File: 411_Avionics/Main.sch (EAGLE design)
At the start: 26 parts, among them CN1 Battery Connector, IC1 BQ24022, IC3 74AC11138D, T1 NTR1P02, T2 NTR1P02, U1 USB_In, U2 ATTINY85V-10SU, U3 LSM9DS0, U5 LM317DCY

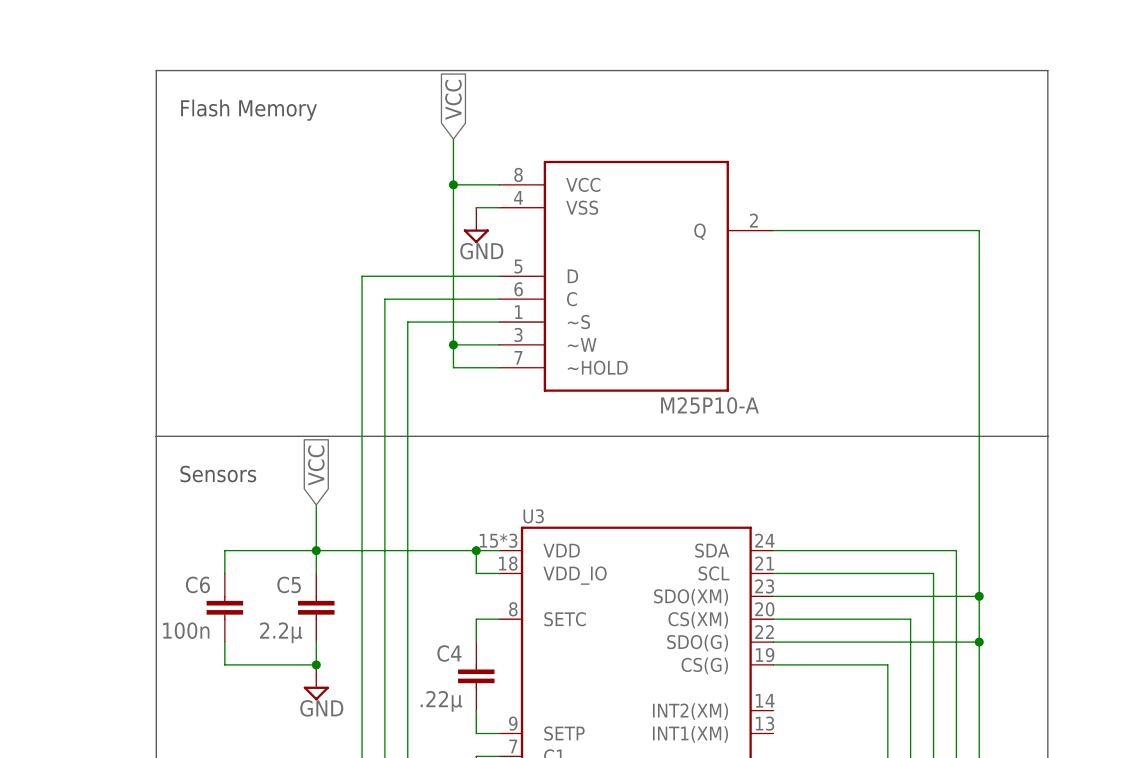
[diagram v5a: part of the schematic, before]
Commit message: Added pin headers to read memory contents. Change before release!
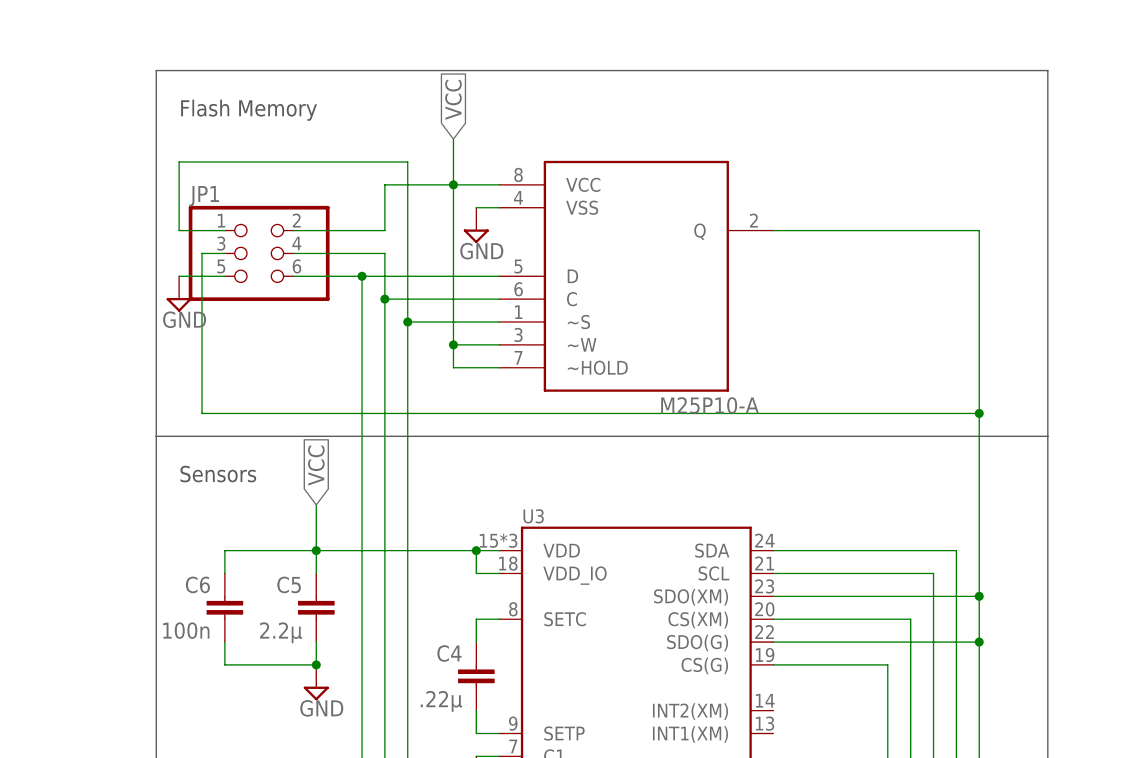
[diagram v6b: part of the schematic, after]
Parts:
- added JP1: (no value), pinhead:PINHD-2X3
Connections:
- net CLK: now also JP1.4
- net GND: now also JP1.5
- net MEM_EN: now also JP1.1
- net MISO: now also JP1.3
- net MOSI: now also JP1.6
- net N$3: now also JP1.2
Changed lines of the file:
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@@
 <part name="C10" library="rcl" deviceset="C-EU" device="C0805" value="100n"/>
 <part name="SUPPLY16" library="supply2" deviceset="GND" device=""/>
+<part name="JP1" library="pinhead" deviceset="PINHD-2X3" device=""/>
+<part name="SUPPLY17" library="supply2" deviceset="GND" device=""/>
 </parts>
 <sheets>
@@
 <instance part="C10" gate="G$1" x="170.18" y="246.38" rot="MR0"/>
 <instance part="SUPPLY16" gate="GND" x="170.18" y="238.76"/>
+<instance part="JP1" gate="A" x="269.24" y="220.98"/>
+<instance part="SUPPLY17" gate="GND" x="261.62" y="215.9"/>
 </instances>
 <busses>
@@
 <pinref part="SUPPLY16" gate="GND" pin="GND"/>
 </segment>
+<segment>
+<pinref part="JP1" gate="A" pin="5"/>
+<wire x1="266.7" y1="218.44" x2="261.62" y2="218.44" width="0.1524" layer="91"/>
+<pinref part="SUPPLY17" gate="GND" pin="GND"/>
+</segment>
 </net>
 <net name="N$4" class="0">
@@
 <wire x1="254" y1="127" x2="284.48" y2="127" width="0.1524" layer="91"/>
 <label x="269.24" y="127" size="1.778" layer="95"/>
+<wire x1="284.48" y1="215.9" x2="284.48" y2="220.98" width="0.1524" layer="91"/>
+<junction x="284.48" y="215.9"/>
+<pinref part="JP1" gate="A" pin="4"/>
+<wire x1="284.48" y1="220.98" x2="274.32" y2="220.98" width="0.1524" layer="91"/>
 </segment>
 </net>
@@
 <pinref part="U$1" gate="G$1" pin="Q"/>
 <wire x1="350.52" y1="177.8" x2="350.52" y2="182.88" width="0.1524" layer="91"/>
-<wire x1="350.52" y1="182.88" x2="350.52" y2="223.52" width="0.1524" layer="91"/>
+<wire x1="350.52" y1="182.88" x2="350.52" y2="203.2" width="0.1524" layer="91"/>
+<wire x1="350.52" y1="203.2" x2="350.52" y2="223.52" width="0.1524" layer="91"/>
 <wire x1="350.52" y1="223.52" x2="327.66" y2="223.52" width="0.1524" layer="91"/>
 <pinref part="U3" gate="G$1" pin="SDO(XM)"/>
@@
 <junction x="350.52" y="177.8"/>
 <label x="269.24" y="129.54" size="1.778" layer="95"/>
+<wire x1="350.52" y1="203.2" x2="264.16" y2="203.2" width="0.1524" layer="91"/>
+<junction x="350.52" y="203.2"/>
+<wire x1="264.16" y1="203.2" x2="264.16" y2="220.98" width="0.1524" layer="91"/>
+<pinref part="JP1" gate="A" pin="3"/>
+<wire x1="264.16" y1="220.98" x2="266.7" y2="220.98" width="0.1524" layer="91"/>
 </segment>
 </net>
@@
 <wire x1="347.98" y1="187.96" x2="327.66" y2="187.96" width="0.1524" layer="91"/>
 <label x="269.24" y="132.08" size="1.778" layer="95"/>
+<pinref part="JP1" gate="A" pin="6"/>
+<wire x1="274.32" y1="218.44" x2="281.94" y2="218.44" width="0.1524" layer="91"/>
+<junction x="281.94" y="218.44"/>
 </segment>
 </net>
@@
 <wire x1="337.82" y1="119.38" x2="325.12" y2="119.38" width="0.1524" layer="91"/>
 <label x="327.66" y="119.38" size="1.778" layer="95"/>
+<wire x1="287.02" y1="213.36" x2="287.02" y2="231.14" width="0.1524" layer="91"/>
+<junction x="287.02" y="213.36"/>
+<wire x1="287.02" y1="231.14" x2="261.62" y2="231.14" width="0.1524" layer="91"/>
+<wire x1="261.62" y1="231.14" x2="261.62" y2="223.52" width="0.1524" layer="91"/>
+<pinref part="JP1" gate="A" pin="1"/>
+<wire x1="261.62" y1="223.52" x2="266.7" y2="223.52" width="0.1524" layer="91"/>
 </segment>
 </net>
@@
 <wire x1="297.18" y1="228.6" x2="292.1" y2="228.6" width="0.1524" layer="91"/>
 <junction x="292.1" y="228.6"/>
-</segment>
-</net>
+<pinref part="JP1" gate="A" pin="2"/>
+<wire x1="274.32" y1="223.52" x2="284.48" y2="223.52" width="0.1524" layer="91"/>
+<wire x1="284.48" y1="223.52" x2="284.48" y2="228.6" width="0.1524" layer="91"/>
+<wire x1="284.48" y1="228.6" x2="292.1" y2="228.6" width="0.1524" layer="91"/>
+</segment>
+</net>

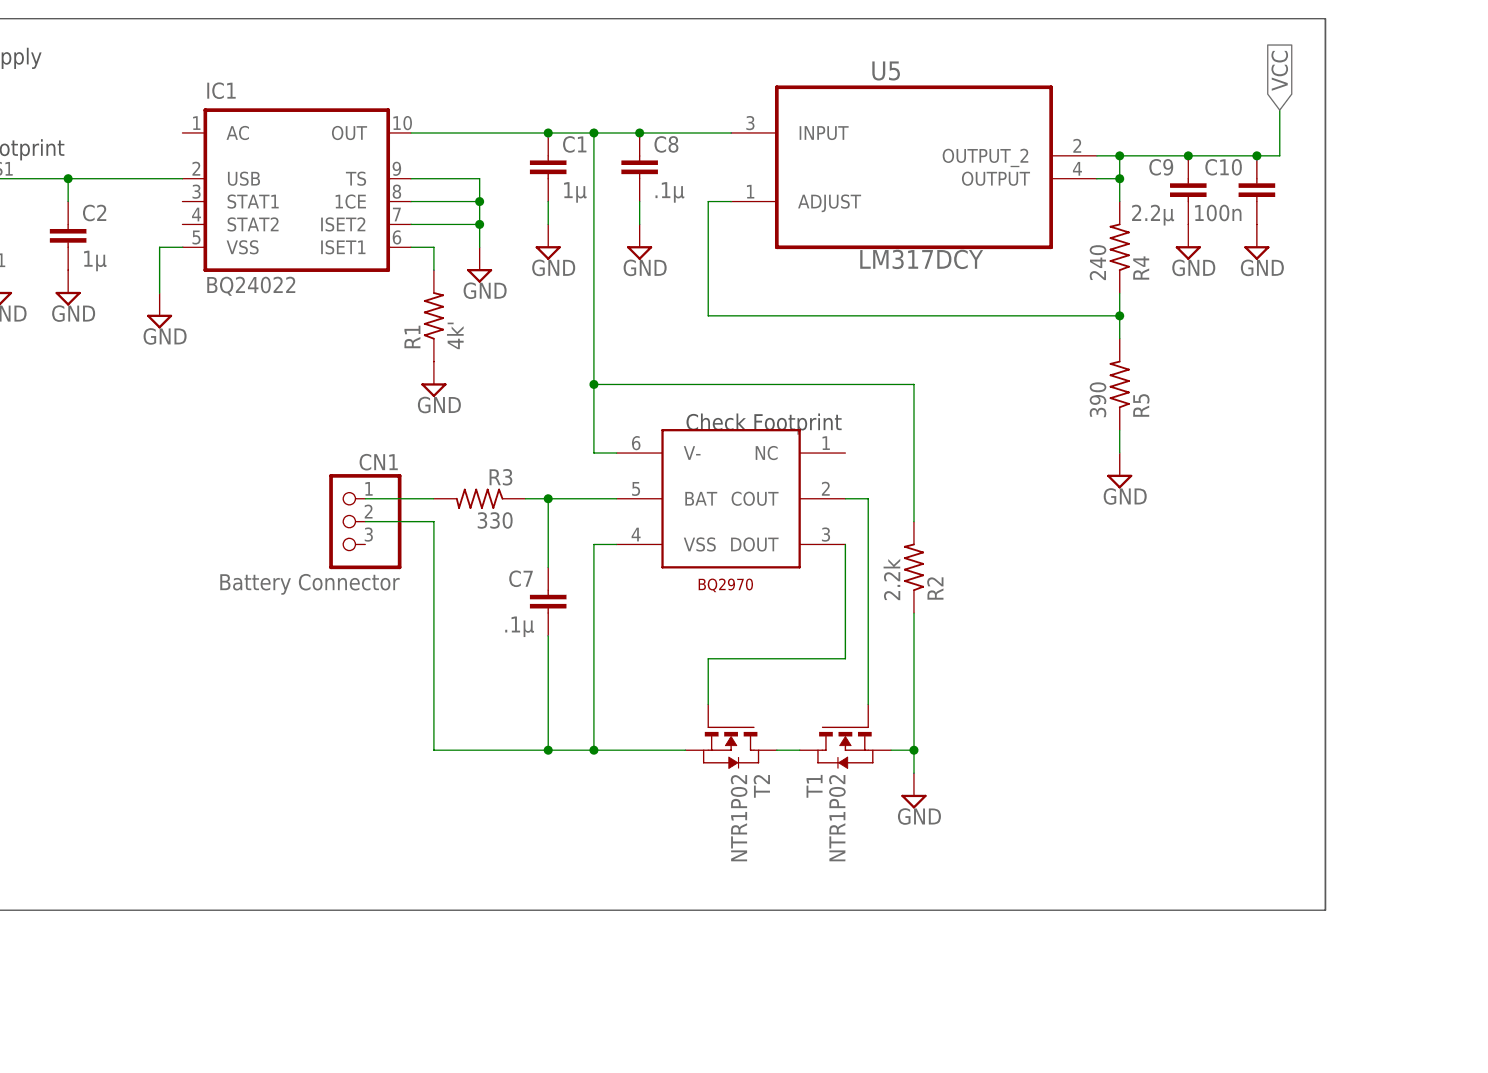
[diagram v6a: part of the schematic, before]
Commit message: ECE411: Began reworking schematic, removed cell protection and added LDO to library and schematic.
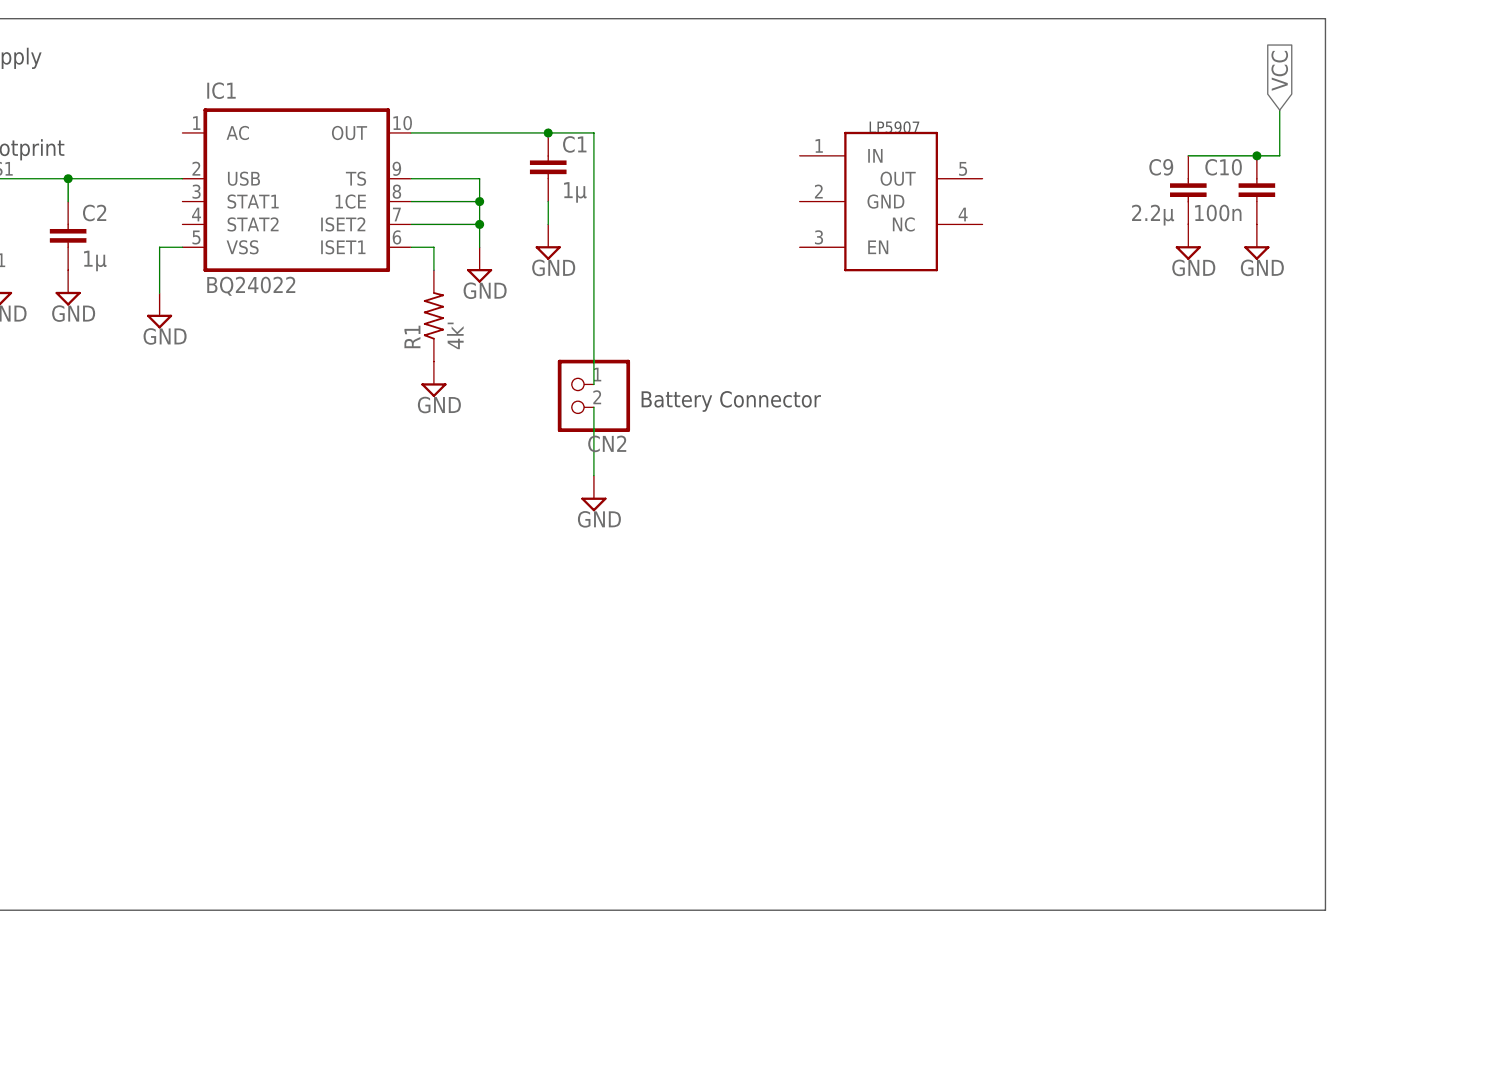
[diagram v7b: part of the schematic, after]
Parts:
- removed C7: .1µ, rcl:C-EUC0805
- removed C8: .1µ, rcl:C-EU050-025X075
- removed CN1: Battery Connector, adafruit:JST_3PIN
- removed R2: 2.2k, resistor:R-US_R0805
- removed R3: 330, resistor:R-US_R0805
- removed R4: 240, resistor:R-US_R0805
- removed R5: 390, resistor:R-US_R0805
- removed T1, T2: NTR1P02, zetex:NMOSSOT23
- removed U5: LM317DCY, LM317DCY:LM317DCY
- added CN2: (no value), adafruit:JST_2PIN-SMT-RA
- U$2: value BQ2970 -> LP5907; device WSON-6-PAD:BQ2970 -> adafruit:LP5907
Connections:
- removed net N$12: T1.G, U$2.COUT
- removed net N$13: T2.G, U$2.DOUT
- removed net N$14: T1.D, T2.D
- removed net N$15: C7.1, R3.1, U$2.BAT
- removed net N$16: C7.2, CN1.2, T2.S, U$2.VSS
- removed net N$18: CN1.1, R3.2
- removed net N$20: R4.1, R5.2, U5.ADJUST
- net GND: now also CN2.1; no longer C8.2, R2.1, R5.1, T1.S
- net N$17: now also CN2.2; no longer C8.1, R2.2, U$2.V-, U5.INPUT
- net VCC: no longer R4.2, U5.OUTPUT, U5.OUTPUT_2
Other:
- note added: "Battery Connector"

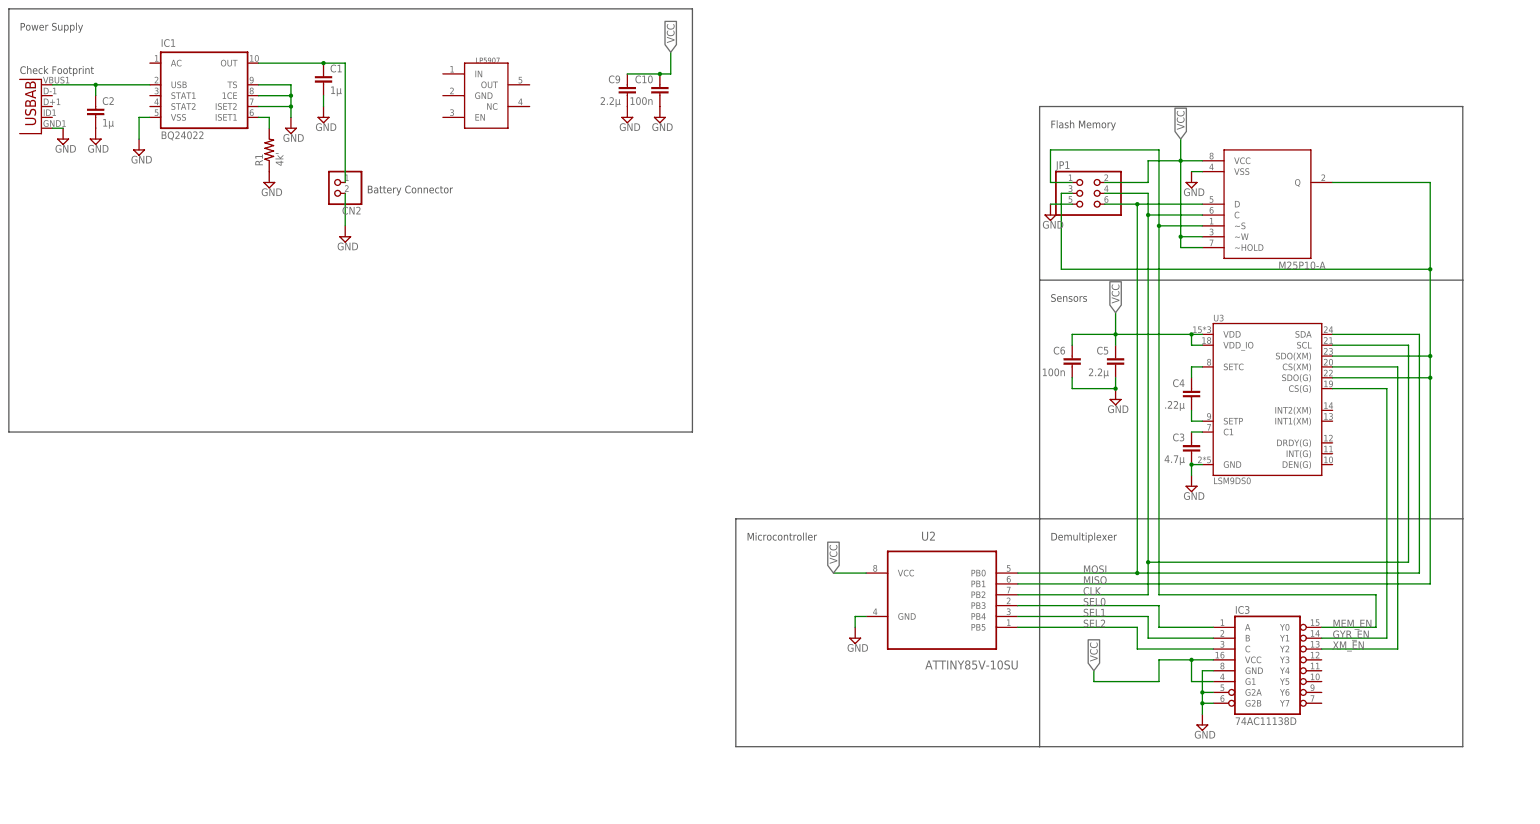
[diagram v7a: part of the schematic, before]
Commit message: Replaced ATTiny with ATMega32U4. Hooked up LDO.
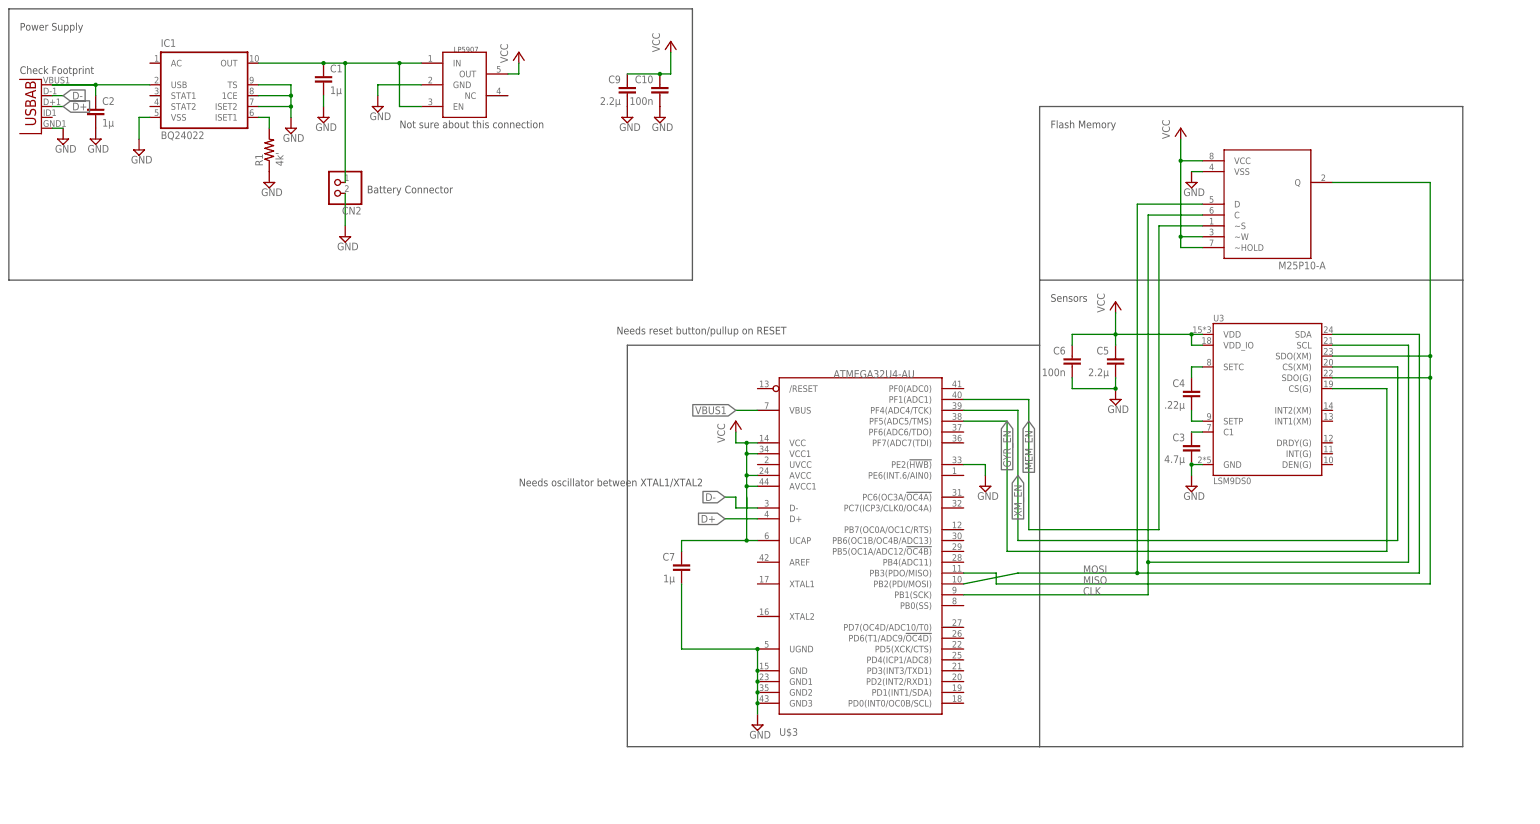
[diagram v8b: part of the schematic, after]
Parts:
- removed IC3: 74AC11138D, 74ac-logic:74AC11138D
- removed JP1: (no value), pinhead:PINHD-2X3
- removed U2: ATTINY85V-10SU, ATTINY85V-10SU:ATTINY85V-10SU
- added C7: 1µ, rcl:C-EUC0805
- added U$3: ATMEGA32U4-AU, adafruit:ATMEGA32U4-AU
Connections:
- removed net N$3: JP1.2, U$1.VCC, U$1.~HOLD, U$1.~W
- removed net N$5: C5.1, C6.1, U3.VDD, U3.VDD_IO
- removed net SEL0: IC3.A, U2.PB3
- removed net SEL1: IC3.B, U2.PB4
- removed net SEL2: IC3.C, U2.PB5
- new net D+: U$3.D+, U1.D+
- new net D-: U$3.D-, U1.D-
- new net VBUS1: U$3.VBUS
- net CLK: now also U$3.PB1(SCK); no longer JP1.4, U2.PB2
- net GND: now also C7.2, U$2.GND, U$3.GND, U$3.GND1, U$3.GND2, U$3.GND3, U$3.PE2(!HWB), U$3.UGND; no longer IC3.G2A, IC3.G2B, IC3.GND, JP1.5, U2.GND
- net GYR_EN: now also U$3.PF5(ADC5/TMS); no longer IC3.Y1
- net MEM_EN: now also U$3.PF1(ADC1); no longer IC3.Y0, JP1.1
- net MISO: now also U$3.PB3(PDO/MISO); no longer JP1.3, U2.PB1
- net MOSI: now also U$3.PB2(PDI/MOSI); no longer JP1.6, U2.PB0
- net N$17: now also U$2.EN, U$2.IN
- net VCC: now also C5.1, C6.1, C7.1, U$1.VCC, U$1.~HOLD, U$1.~W, U$2.OUT, U$3.AVCC, U$3.AVCC1, U$3.UCAP, U$3.VCC, U$3.VCC1, U3.VDD, U3.VDD_IO; no longer IC3.G1, IC3.VCC, U2.VCC
- net XM_EN: now also U$3.PF4(ADC4/TCK); no longer IC3.Y2
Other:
- note added: "Needs oscillator between XTAL1/XTAL2"
- note added: "Needs reset button/pullup on RESET"
- note added: "Not sure about this connection"
- note removed: "Demultiplexer"
- note removed: "Microcontroller"
